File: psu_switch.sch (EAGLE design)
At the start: 12 parts, among them K1 OMRON-G3MB-202P-SSR, T1 BC547

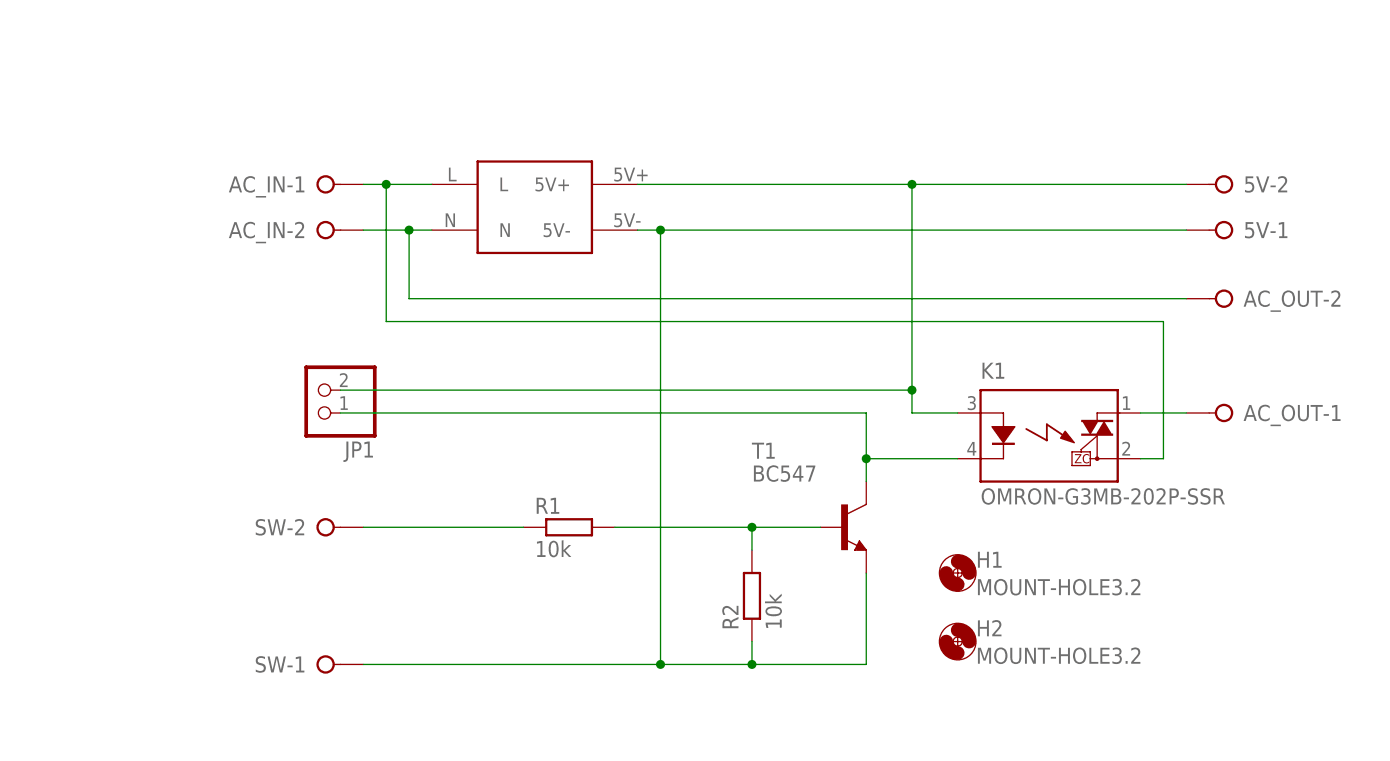
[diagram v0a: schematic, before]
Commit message: Fix label and add GERBER files for PSU switch.
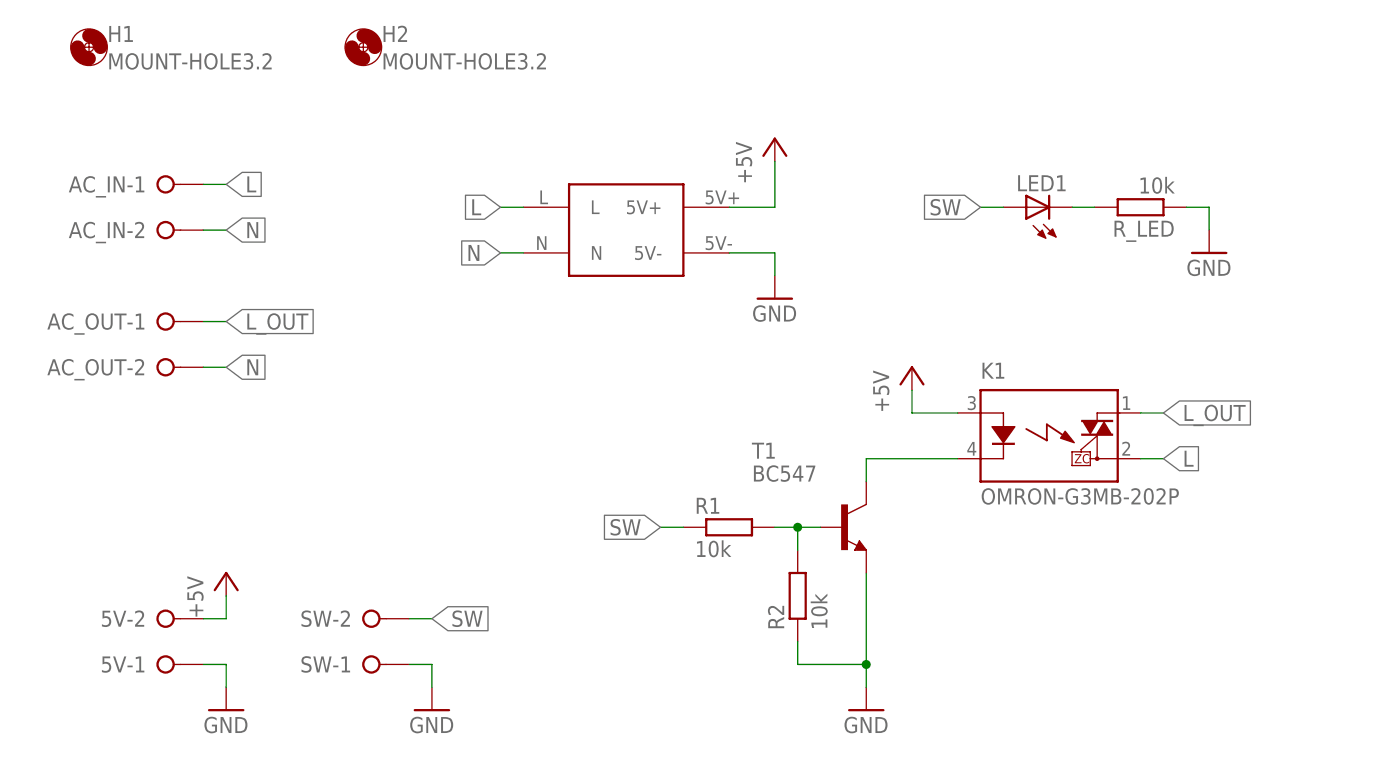
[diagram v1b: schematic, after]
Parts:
- removed JP1: (no value), pinhead:PINHD-1X2
- added LED1: (no value), led:LED3MM
- added R_LED: 10k, resistor:R-EU_0207/10
- K1: value OMRON-G3MB-202P-SSR -> OMRON-G3MB-202P
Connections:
- net N$1 renamed L_OUT
- removed net 5V+: 5V-2.KL, JP1.2, K1.A, U$1.5V+
- removed net N$2: R1.1, SW-2.KL
- new net +5V: 5V-2.KL, K1.A, U$1.5V+
- new net N$1: LED1.C, R_LED.2
- new net SW: LED1.A, R1.1, SW-2.KL
- net GND: now also R_LED.1
- net N$5: no longer JP1.1
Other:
- moved on the sheet: 5V-1, 5V-2, AC_IN-1, AC_IN-2, AC_OUT-1, AC_OUT-2, H1, H2, R1, R2, SW-1, SW-2
